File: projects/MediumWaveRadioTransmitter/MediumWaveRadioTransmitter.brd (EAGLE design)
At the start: 32.7 x 40.6 mm, 20 parts, among them P4 100k, Q1 400kH, T1 BC337, T2 BC337

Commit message: fix: mwrt fixed a little bit
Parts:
- removed 12V, GND, TP1, TP2, TP3: SE13, solpad:SE13
- added X1: IN_OUT, con-wago-508:W237-5P
- T1, T2: device transistor:TO92 -> transistor:TO92-CBE
- moved R5 60.2 mm to (7.62, 20.3)
- moved R6 54.0 mm to (7.62, 17.8)
- moved R7 53.9 mm to (7.62, 15.2)
- moved T2 52.9 mm to (25.4, 16.5)
- moved R2 51.9 mm to (8.89, 30.5)
- moved T1 50.1 mm to (17.8, 16.5)
- moved R9 47.7 mm to (21.6, 12.7), turned to 180 degrees
- moved R8 44.5 mm to (8.89, 12.7), turned to 180 degrees
- moved R1 39.2 mm to (8.89, 27.9)
- moved R3 39.2 mm to (8.89, 33.0)
- moved Q1 38.2 mm to (20.3, 22.9), turned to 0 degrees
- moved P4 36.7 mm to (8.89, 24.1)
- moved C2 29.0 mm to (17.8, 30.5), turned to 0 degrees
- moved C1 26.1 mm to (17.8, 27.9), turned to 0 degrees
- moved C3 19.3 mm to (17.8, 33.0), turned to 0 degrees
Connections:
- removed net N$4: C1.2, C2.2, C3.2, GND.MP, P4.1, Q1.2, R8.1, R9.1
- new net GND: C1.2, C2.2, C3.2, P4.1, Q1.2, R8.1, R9.1, X1.5
- net N$10: now also T2.C, X1.3; no longer T2.3, TP2.MP
- net N$3: now also T1.B; no longer T1.2
- net N$5: now also T1.C, T2.B, X1.2; no longer T1.3, T2.2, TP1.MP
- net N$6: now also T1.E; no longer T1.1
- net N$7: now also X1.1; no longer 12V.MP
- net N$8: now also T2.E, X1.4; no longer T2.1, TP3.MP
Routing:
- net N$4: track 54.9 -> 0.00 mm
- net GND: track 0.00 -> 52.9 mm
- net N$7: track 61.3 -> 20.7 mm
- net N$3: track 73.9 -> 41.7 mm
- net N$10: track 52.9 -> 34.5 mm
- net N$2: track 30.0 -> 13.8 mm
- net N$8: track 37.4 -> 23.1 mm
- net N$5: track 64.6 -> 53.1 mm
- net N$1: track 20.2 -> 13.8 mm
- net N$6: track 22.4 -> 18.1 mm
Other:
- board size 32.7 x 40.6 mm -> 30.5 x 35.5 mm

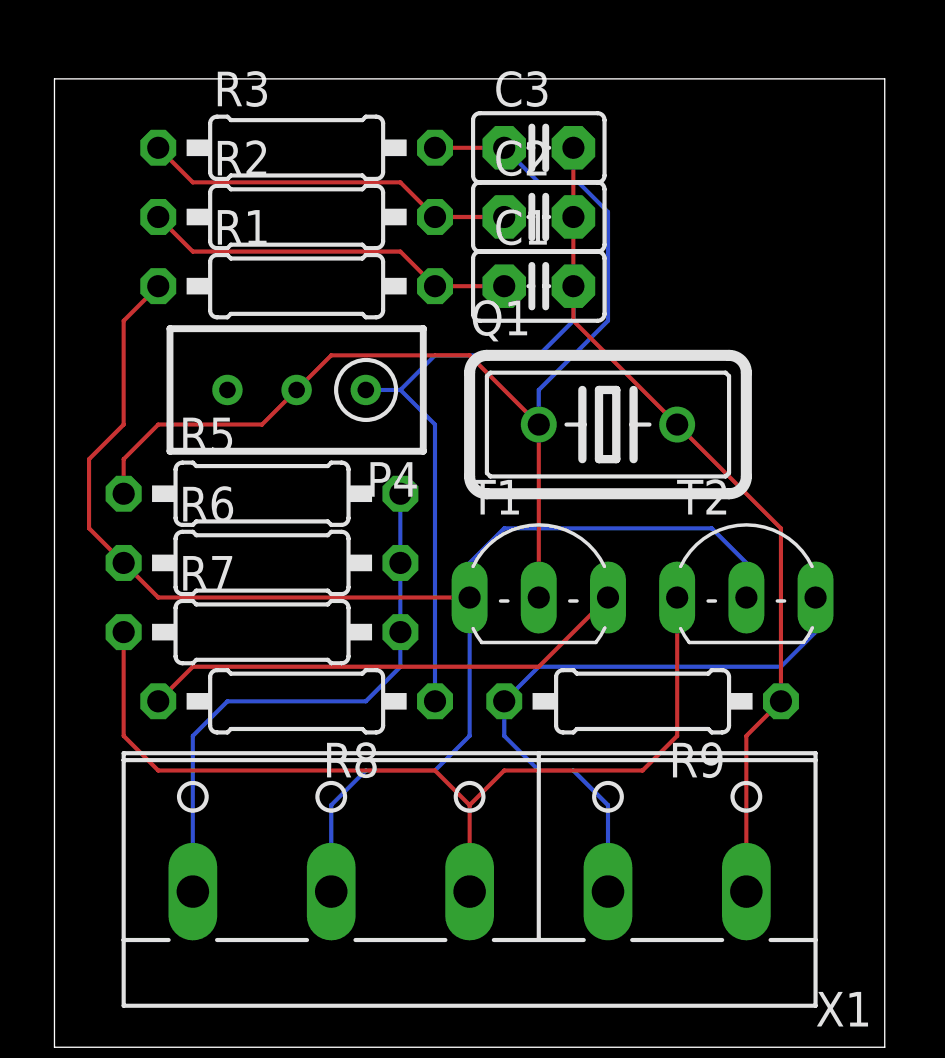
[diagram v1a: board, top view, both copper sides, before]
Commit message: fix: Medium Wave Radio Transmitter fixes applied
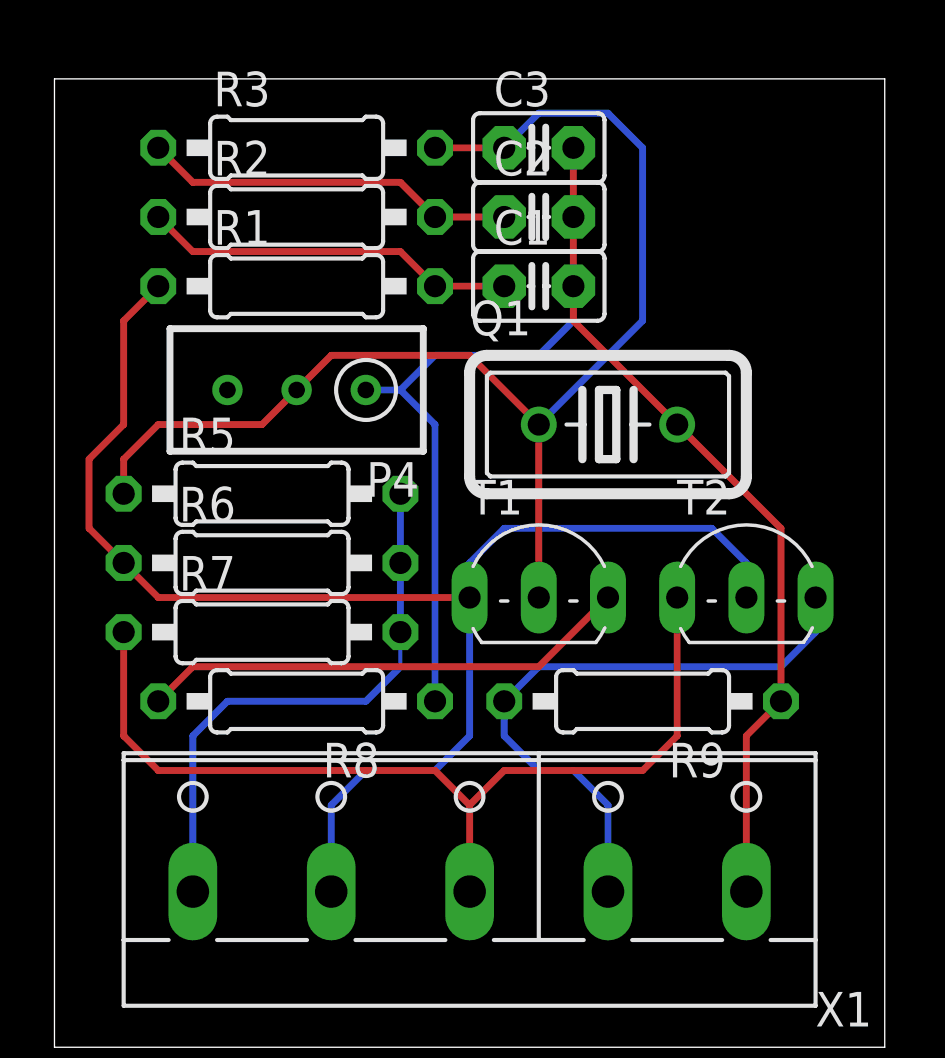
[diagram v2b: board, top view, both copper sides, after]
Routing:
- net N$3: track 41.7 -> 45.9 mm

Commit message: feat: medium wave transmiter gerber added
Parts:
- moved R7 1.27 mm to (7.62, 16.5)
- moved R8 1.27 mm to (8.89, 14.0)
- moved R9 1.27 mm to (21.6, 14.0)
- moved X1 1.27 mm to (15.2, 7.62)
- moved C1 1.27 mm to (17.8, 29.2)
- moved C2 1.27 mm to (17.8, 31.8)
- moved P4 1.27 mm to (8.89, 25.4)
- moved Q1 1.27 mm to (20.3, 24.1)
- moved R1 1.27 mm to (8.89, 29.2)
- moved R2 1.27 mm to (8.89, 31.8)
- moved R5 1.27 mm to (7.62, 21.6)
- moved R6 1.27 mm to (7.62, 19.1)
- moved T1 1.27 mm to (17.8, 17.8)
- moved T2 1.27 mm to (25.4, 17.8)
- moved C3 1.27 mm to (17.8, 34.3)
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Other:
- board size 30.5 x 35.5 mm -> 30.5 x 38.1 mm

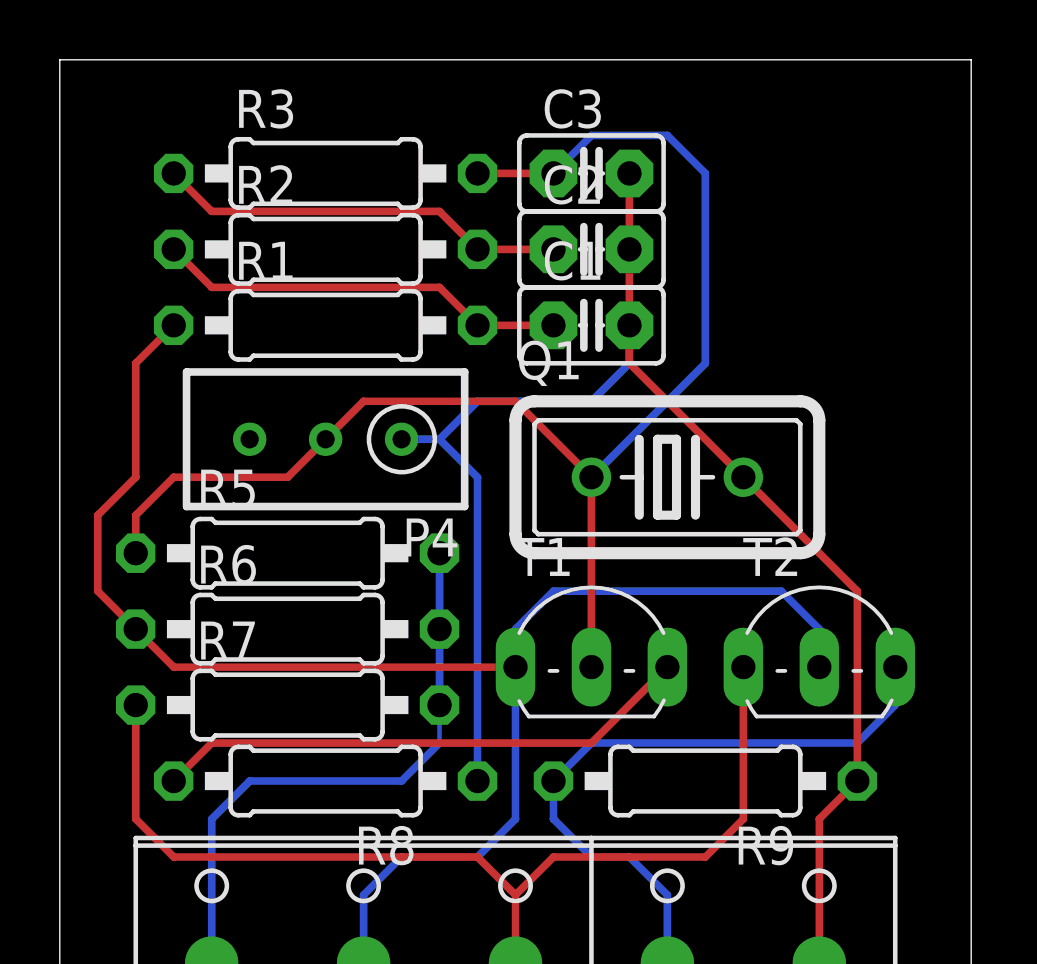
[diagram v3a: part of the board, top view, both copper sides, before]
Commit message: fix: medium wave radio transmitter
changes:
- schematic fixed (capacitor packages)
- routing fixed (capacitor packages)
- new gerber files added
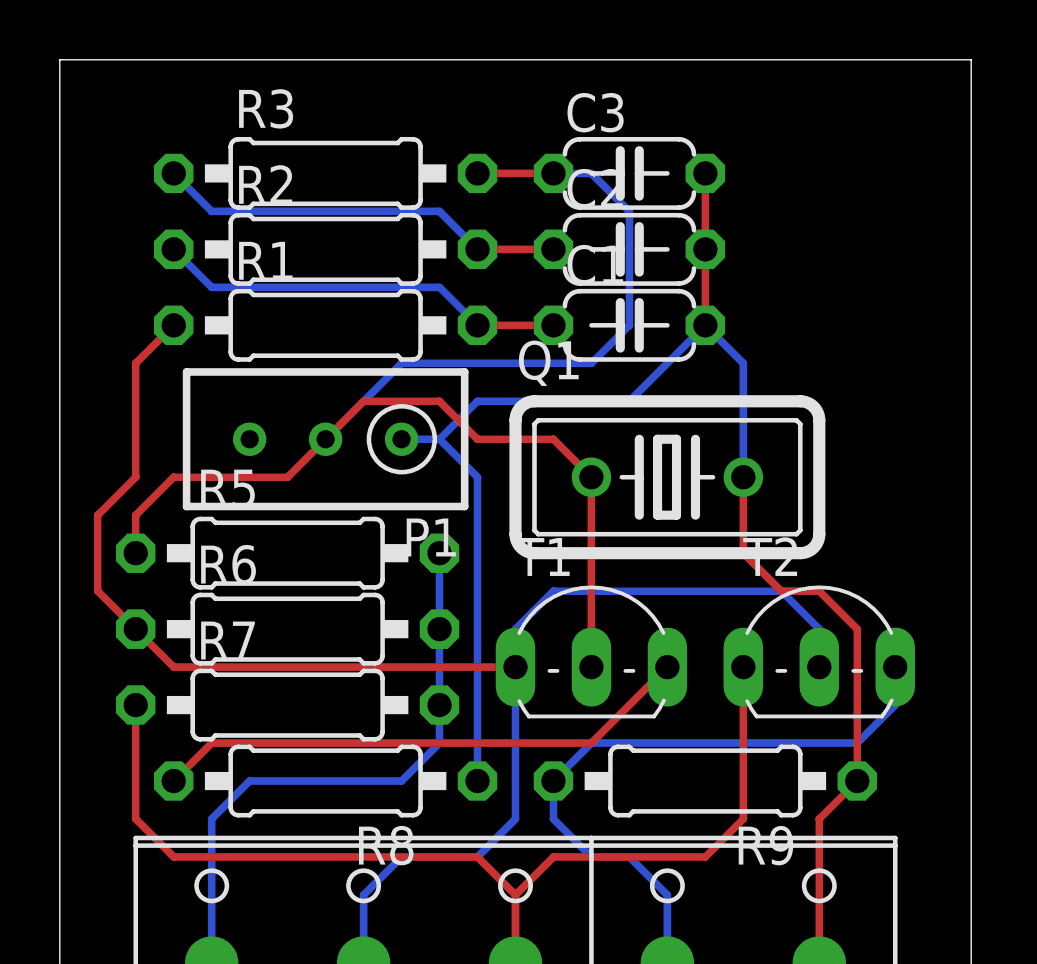
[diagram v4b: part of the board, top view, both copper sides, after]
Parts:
- C1, C2, C3: device capacitor-wima:C2.5-2 -> rcl:C050-024X044
- moved C1 1.27 mm to (19.1, 29.2)
- moved C2 1.27 mm to (19.1, 31.8)
- moved C3 1.27 mm to (19.1, 34.3)
- renumbered P4 to P1
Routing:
- net GND: track 52.9 -> 54.4 mm
- net N$3: track 45.9 -> 46.6 mm

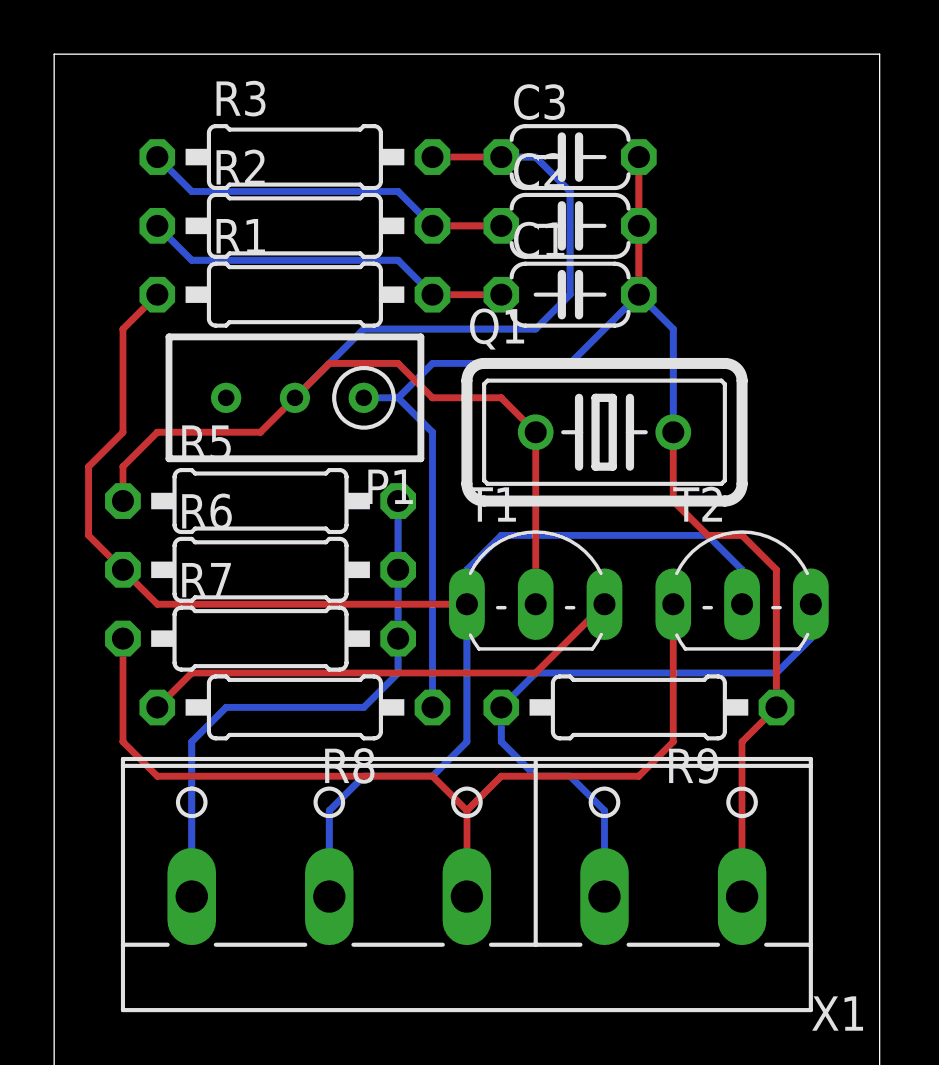
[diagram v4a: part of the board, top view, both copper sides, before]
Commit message: fix: mwrt and led control fixed
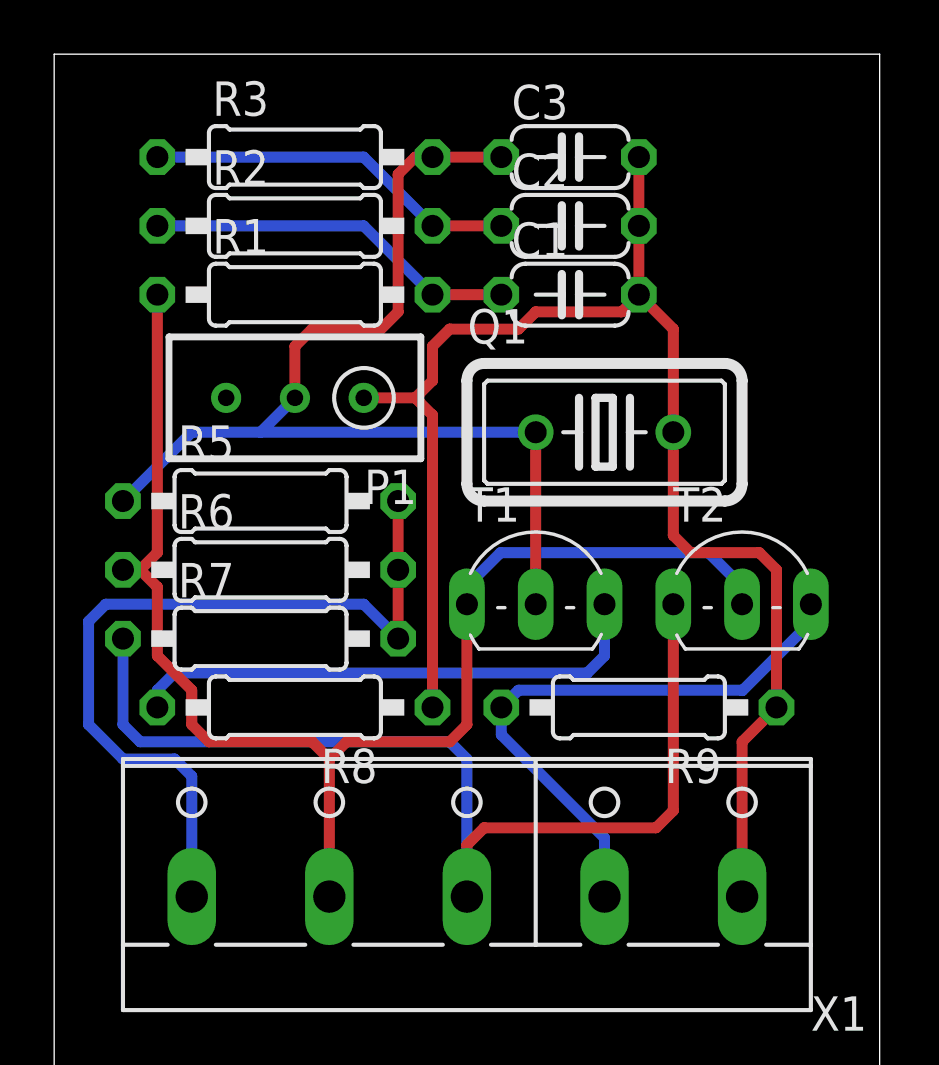
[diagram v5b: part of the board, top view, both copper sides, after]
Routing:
- net N$7: track 20.7 -> 30.2 mm
- net N$3: track 46.6 -> 39.8 mm
- net N$10: track 34.5 -> 39.2 mm
- net N$5: track 53.1 -> 50.8 mm
- net N$6: track 18.1 -> 19.6 mm
- net GND: track 54.4 -> 55.6 mm
- net N$8: track 23.1 -> 22.0 mm
